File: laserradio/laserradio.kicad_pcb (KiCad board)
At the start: 2 copper layers, 84 parts, among them J1 USB4105-GF-A, J2 Conn_01x01_Female, J3 DEBUG, J4 RIGHT, SW1 SW_SPDT, SW2 SW_SPDT, U1 W25Q128JV, U2 RP2040, U3 MCP1702T-3302E_CB, U4 ADA4891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

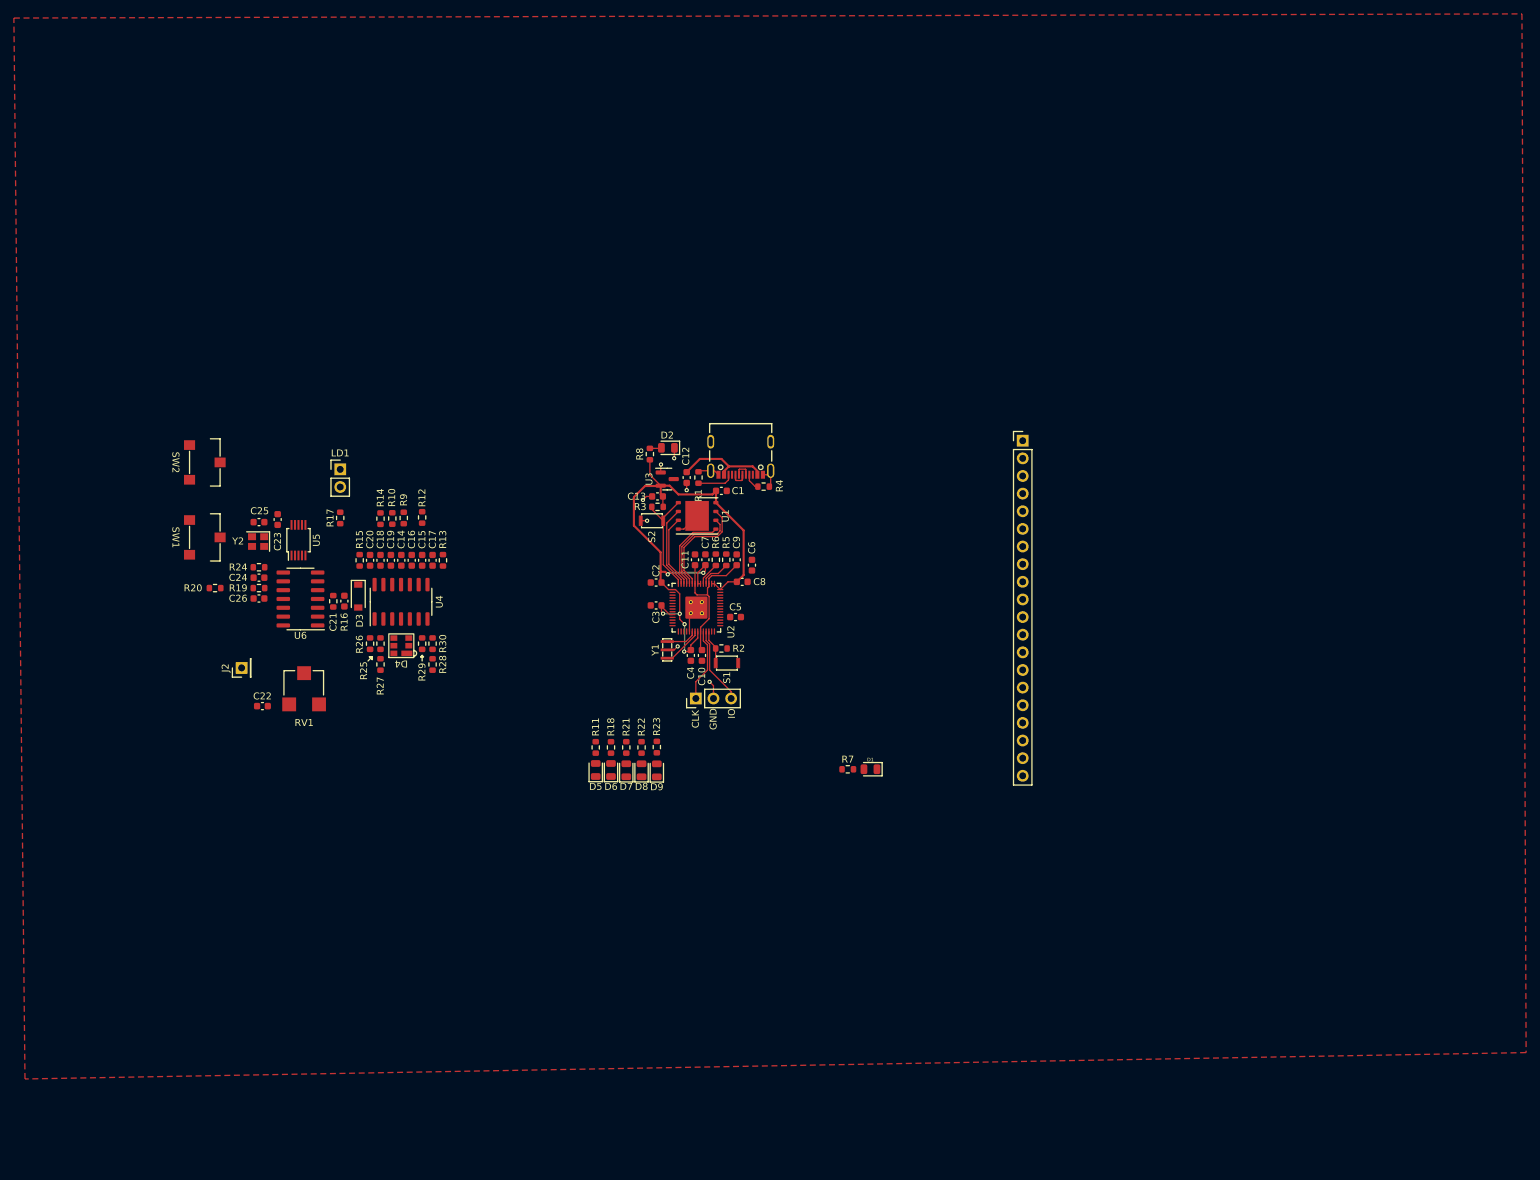
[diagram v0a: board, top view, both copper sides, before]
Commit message: update schematic
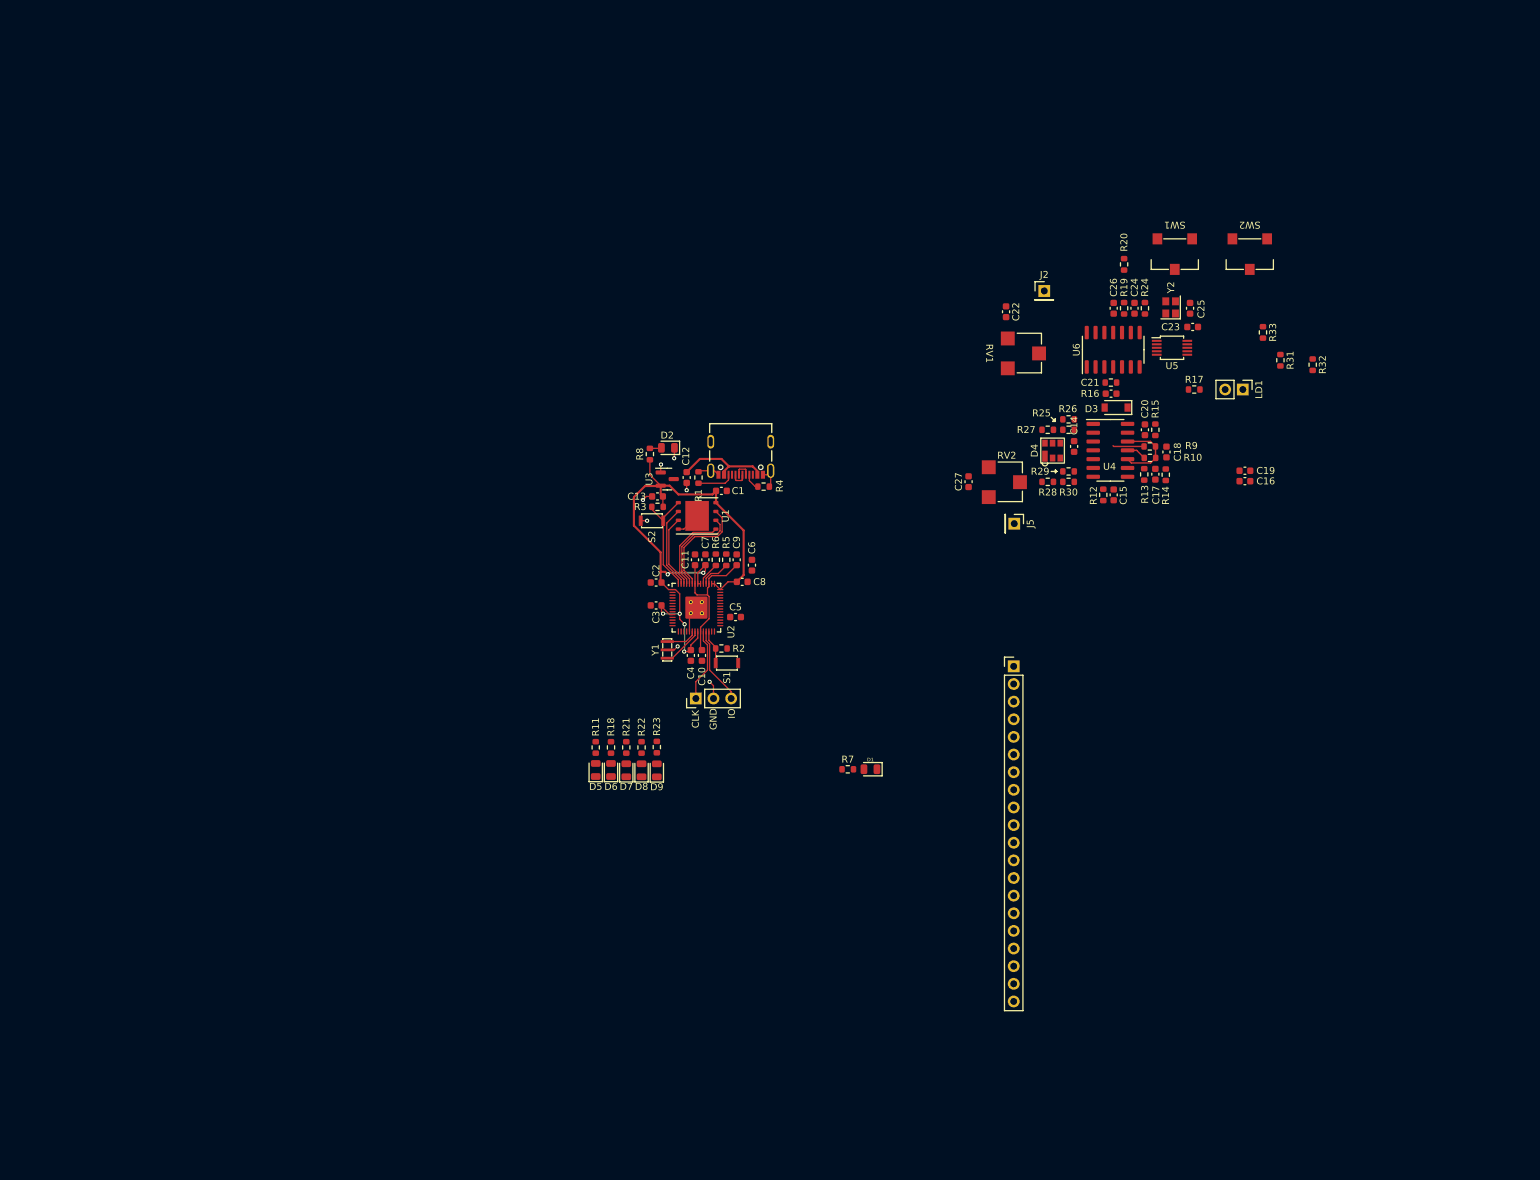
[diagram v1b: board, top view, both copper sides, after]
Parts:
- added C27: 10pF, Capacitor_SMD:C_0603_1608Metric, F.Cu at (153.5, 81.8)
- added J5: Conn_01x01_Female, Connector_PinHeader_2.54mm:PinHeader_1x01_P2.54mm_Vertical, F.Cu at (160.1, 87.8)
- added R31: 20k, Resistor_SMD:R_0603_1608Metric, F.Cu at (198.4, 64.3)
- added R32: 5k, Resistor_SMD:R_0603_1608Metric, F.Cu at (203.1, 64.9)
- added R33: 10k, Resistor_SMD:R_0603_1608Metric, F.Cu at (195.9, 60.3)
- added RV2: Nominal 10k, Eclectronics:Laser Potentiometer, F.Cu at (158.7, 81.8)
- R20: value 10k -> 20k
- moved SW2 153.5 mm to (194.0, 49.0), turned to 180 degrees
- moved SW1 145.5 mm to (183.2, 49.0), turned to 180 degrees
- moved R20 139.0 mm to (175.9, 50.5), turned to 90 degrees
- moved C25 137.6 mm to (185.4, 56.8), turned to 90 degrees
- moved Y2 135.7 mm to (182.6, 56.7), turned to 90 degrees
- moved C23 134.7 mm to (185.8, 59.5), turned to 0 degrees
- moved R24 132.9 mm to (178.9, 56.8), turned to -90 degrees
- moved C24 131.9 mm to (177.4, 56.8), turned to -90 degrees
- moved R19 131.0 mm to (175.9, 56.8), turned to 90 degrees
- moved LD1 130.5 mm to (193.0, 68.5), turned to -90 degrees
- moved C26 130.0 mm to (174.4, 56.8), turned to 90 degrees
- moved U5 128.8 mm to (182.8, 62.5), turned to 0 degrees
- moved J2 127.7 mm to (164.4, 54.3), turned to 0 degrees
- moved R17 124.4 mm to (186.0, 68.5), turned to 0 degrees
- moved C19 123.7 mm to (193.3, 80.2), turned to 0 degrees
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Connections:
- C24 pad 2: Net-(C24-Pad2) -> GND
- R19 pad 1: Net-(C24-Pad2) -> Net-(R19-Pad1)
- R24 pad 1: Net-(C24-Pad1) -> Net-(Y2-Pad3)
- R24 pad 2: Net-(C24-Pad2) -> Net-(C24-Pad1)
- R28 pad 1: Net-(R26-Pad2) -> Net-(R28-Pad1)
- R29 pad 1: Net-(R26-Pad2) -> Net-(R28-Pad1)
- U4 pad 5: GND -> Net-(R28-Pad1)
- U5 pad 1: Net-(R19-Pad2) -> Net-(U5-Pad1)
- U5 pad 2: Net-(C24-Pad2) -> Net-(R19-Pad1)
- U6 pad 12: unconnected-(U6-Pad12) -> Net-(R19-Pad1)
- U6 pad 13: unconnected-(U6-Pad13) -> Net-(U6-Pad13)
- U6 pad 14: unconnected-(U6-Pad14) -> Net-(U6-Pad13)
- U6 pad 8: Net-(C24-Pad2) -> Net-(R19-Pad1)
- Y2 pad 3: Net-(C24-Pad1) -> Net-(Y2-Pad3)
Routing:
- net /VCENTER: track 0.00 -> 10.6 mm
- net +3V3: track 87.5 -> 92.0 mm
- net GND: track 24.8 -> 27.6 mm
- removed copper zone on F.Cu, net (none)

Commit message: Mid work upload
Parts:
- moved R32 128.8 mm to (74.6, 74.4), turned to 90 degrees
- moved R33 123.6 mm to (73.1, 74.4)
- moved C25 118.6 mm to (72.4, 92.8), turned to 0 degrees
- moved SW2 115.6 mm to (82.5, 79.5), turned to 90 degrees
- moved Y2 110.6 mm to (72.6, 68.3), turned to 180 degrees
- moved C15 108.7 mm to (67.1, 101.2)
- moved C16 108.7 mm to (86.0, 99.3)
- moved C17 108.7 mm to (73.1, 98.3)
- moved C19 108.7 mm to (86.0, 97.8)
- moved C21 108.7 mm to (66.8, 86.7)
- moved C23 108.7 mm to (78.5, 77.0)
- moved C24 108.7 mm to (70.1, 74.4)
- moved C26 108.7 mm to (67.1, 74.4)
- moved J5 108.7 mm to (52.8, 105.4)
- moved R12 108.7 mm to (65.6, 101.2)
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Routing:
- net /VCENTER: track 10.6 -> 4.58 mm
- net +3V3: track 92.0 -> 87.5 mm
- net Net-(LD1-Pad2): track 0.00 -> 3.03 mm
- net GND: track 27.6 -> 28.7 mm, vias 7 -> 8

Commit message: Major layout changes
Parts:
- removed C16: 10µF, Capacitor_SMD:C_0603_1608Metric
- removed J2, J5: Conn_01x01_Female, Connector_PinHeader_2.54mm:PinHeader_1x01_P2.54mm_Vertical
- added C28: 10pF, Capacitor_SMD:C_0603_1608Metric, F.Cu at (78.6, 81.4)
- added Rx-Center1: Conn_01x01_Female, Connector_PinHeader_2.54mm:PinHeader_1x01_P2.54mm_Vertical, F.Cu at (72.7, 110.1)
- added Rx-Thresh1: Conn_01x01_Female, Connector_PinHeader_2.54mm:PinHeader_1x01_P2.54mm_Vertical, F.Cu at (71.6, 84.9)
- moved C22 26.5 mm to (69.3, 94.6)
- moved C27 22.7 mm to (66.4, 109.9), turned to 0 degrees
- moved RV1 22.1 mm to (73.7, 91.2)
- moved Y2 20.7 mm to (89.3, 80.6), turned to 90 degrees
- moved C18 19.1 mm to (92.8, 101.5)
- moved R14 18.5 mm to (92.0, 104.7)
- moved C17 18.4 mm to (90.4, 104.7)
- moved C20 18.4 mm to (88.8, 97.0)
- moved R13 18.4 mm to (88.8, 104.7)
- moved R15 18.4 mm to (90.3, 97.0)
- moved R9 18.4 mm to (89.6, 100.7)
- moved C25 18.4 mm to (89.6, 99.2)
- moved R10 18.4 mm to (89.6, 102.3)
- moved RV2 17.6 mm to (67.9, 105.7)
- moved C21 16.6 mm to (82.0, 93.1)
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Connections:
- R28 pad 1: Net-(R28-Pad1) -> Net-(Rx-Center1-Pad1)
- R29 pad 1: Net-(R28-Pad1) -> Net-(Rx-Center1-Pad1)
- RV2 pad 2: Net-(R28-Pad1) -> Net-(Rx-Center1-Pad1)
- U4 pad 5: Net-(R28-Pad1) -> Net-(R26-Pad2)
- U4 pad 6: Net-(R26-Pad2) -> Net-(Rx-Center1-Pad1)
- U6 pad 10: Net-(R19-Pad2) -> Net-(C24-Pad1)
- U6 pad 9: Net-(C24-Pad1) -> Net-(R19-Pad2)
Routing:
- net GND: track 28.7 -> 73.8 mm, vias 8 -> 28
- net Net-(R19-Pad1): track 0.00 -> 20.4 mm
- net Net-(R32-Pad1): track 0.00 -> 16.5 mm
- net Net-(Rx-Center1-Pad1): track 0.00 -> 16.2 mm
- net Net-(Rx-Thresh1-Pad1): track 0.00 -> 13.2 mm
- net Net-(C18-Pad2): track 0.00 -> 11.2 mm
- net Net-(C15-Pad2): track 0.00 -> 10.4 mm
- net Net-(C21-Pad1): track 0.00 -> 10.4 mm
- net Net-(R19-Pad2): track 0.00 -> 10.0 mm, vias 0 -> 2
- net /VBUS: track 13.2 -> 22.8 mm
- net Net-(D4-Pad1): track 0.00 -> 9.47 mm
- net Net-(C20-Pad2): track 0.00 -> 8.77 mm
- net Net-(SW1-Pad2): track 0.00 -> 8.14 mm
- net +3V3: track 87.5 -> 95.5 mm
- net /VCENTER: track 4.58 -> 11.7 mm
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- added copper zone on B.Cu, net GND
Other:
- board text added: "Light"
- board text added: "Safety"

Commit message: Major PCB changes
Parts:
- moved SW1 4.55 mm to (99.9, 95.2)
- moved D7 2.53 mm to (103.3, 109.2)
- moved D8 2.53 mm to (105.5, 109.2)
- moved D9 2.53 mm to (107.7, 109.2)
- moved D6 2.53 mm to (101.1, 109.2)
- moved R18 2.53 mm to (101.1, 106.0)
- moved R21 2.53 mm to (103.3, 106.0)
- moved R22 2.53 mm to (105.5, 106.0)
- moved R23 2.53 mm to (107.7, 105.9)
- moved D5 2.53 mm to (98.9, 109.2)
- moved R11 2.53 mm to (98.9, 106.0)
- moved J3 0.97 mm to (114.2, 112.0)
- moved C23 0.74 mm to (93.2, 83.0), turned to 90 degrees
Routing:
- net +3V3: track 95.5 -> 178.9 mm, vias 6 -> 4
- net /Rx: track 0.00 -> 39.9 mm, vias 0 -> 2
- net /Tx: track 0.00 -> 24.9 mm
- net /Tx_ENABLE: track 0.00 -> 24.9 mm
- net /GPIO8: track 0.00 -> 13.5 mm
- net /GPIO9: track 0.00 -> 11.2 mm
- net GND: track 73.8 -> 84.1 mm, vias 28 -> 30
- net /GPIO10: track 0.00 -> 8.81 mm
- net /GPIO11: track 0.00 -> 6.44 mm
- net /GPIO12: track 0.00 -> 4.71 mm
- net Net-(SW1-Pad2): track 8.14 -> 12.4 mm, vias 0 -> 2
- net Net-(D9-Pad2): track 0.00 -> 1.59 mm
- net Net-(D8-Pad2): track 0.00 -> 1.52 mm
- net Net-(D7-Pad2): track 0.00 -> 1.52 mm
- net Net-(D6-Pad2): track 0.00 -> 1.49 mm
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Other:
- board text added: "BOOT"
- board text added: "LIGHT"
- board text added: "RUN"
- board text added: "SAFETY"
- board text removed: "Light"
- board text removed: "Safety"

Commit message: WIP
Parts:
- removed D1: LED, LED_SMD:LED_0805_2012Metric
- removed R7: 1K, Resistor_SMD:R_0603_1608Metric
- J4: footprint Connector_PinHeader_2.54mm:PinHeader_1x20_P2.54mm_Vertical -> Connector_PinHeader_2.54mm:PinHeader_1x15_P2.54mm_Vertical
- moved J4 42.5 mm to (130.2, 78.0)
- moved C5 0.47 mm to (120.4, 101.2)
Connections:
- J4 pad 14: /GPIO20 -> GND
- J4 pad 15: /GPIO19 -> /RUN
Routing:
- net +3V3: track 178.9 -> 296.3 mm, vias 4 -> 10
- net /VBUS: track 22.6 -> 123.7 mm
- net /RUN: track 4.95 -> 22.4 mm
- net /GPIO21: track 0.00 -> 15.4 mm
- net /GPIO22: track 0.00 -> 14.7 mm
- net Net-(J1-PadA7): track 2.52 -> 15.1 mm
- net Net-(J1-PadA6): track 3.13 -> 15.7 mm
- net GND: track 84.1 -> 90.4 mm, vias 30 -> 36
- net Net-(C17-Pad2): track 6.18 -> 7.82 mm
- net /GPIO29: track 0.00 -> 1.27 mm

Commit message: Completed Initial Draft
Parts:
- added OlinLogoLg: G***, Eclectronics:OlinLogoLg, F.Cu at (73.6, 101.3)
- moved C1 1.30 mm to (119.0, 83.8), turned to -90 degrees
- moved C23 1.14 mm to (92.3, 83.7), turned to 180 degrees
- moved LD1 0.49 mm to (103.3, 87.6)
- moved R15 0.21 mm to (90.4, 96.8)
- moved C20 0.20 mm to (88.8, 96.8)
- moved C25 0.10 mm to (89.6, 99.1)
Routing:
- net /GPIO29: track 1.27 -> 108.6 mm, vias 0 -> 2
- net /BOOT: track 16.2 -> 40.8 mm, vias 0 -> 2
- net /VBUS: track 123.7 -> 143.3 mm, vias 0 -> 2
- net /GPIO28: track 0.00 -> 15.5 mm
- net /GPIO27: track 0.00 -> 14.6 mm
- net /GPIO23: track 0.00 -> 13.8 mm
- net /GPIO26: track 0.00 -> 13.8 mm
- net Net-(R26-Pad2): track 2.99 -> 16.4 mm
- net /GPIO24: track 0.00 -> 12.9 mm
- net GND: track 90.4 -> 99.9 mm, vias 36 -> 42
- net +3V3: track 296.3 -> 291.4 mm
- net Net-(C15-Pad1): track 0.00 -> 1.52 mm
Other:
- board outline added: 68.6 x 43.7 mm
- board text added: "21"
- board text added: "22"
- board text added: "23"
- board text added: "24"
- board text added: "26"
- board text added: "27"
- board text added: "28"
- board text added: "3.3V"
- board text added: "Eclectronics F2022"
- board text added: "Ian Eykamp Braden Oh"
- board text added: "Laser Radio"
- board text added: "Peak Detect"
- board text added: "VBUS"
